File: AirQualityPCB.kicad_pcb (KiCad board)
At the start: 2 copper layers, 100 x 75 mm, 57 parts, among them J1 USB_C_Receptacle_USB2.0_16P, J10 SMA-J-P-H-ST-EM1, J2 TestPoint 5V, J3 TestPoint GND, J4 TestPoint 3.3V, U1 Regulator, U10 INIR2-ME5, U11 110-507, U12 110-303, U13 ESP32-C3-WROOM-02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

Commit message: Updated silkscreen
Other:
- board text added: "LoRa Antenna"
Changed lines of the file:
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@@
+		)
+	)
+	(gr_text "LoRa Antenna"
+		(at 150 65 0)
+		(layer "B.SilkS")
+		(effects
+			(font
+				(size 1.5 1.5)
+				(thickness 0.3)
+				(bold yes)
+			)
+			(justify left bottom mirror)
 		)
 	)

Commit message: Before routing
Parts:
- moved J2 89.5 mm to (296.4, 74.5)
- moved J3 89.5 mm to (292.4, 74.5)
- moved J4 89.5 mm to (288.4, 74.5)
- moved R7 89.5 mm to (284.4, 105.9)
- moved U10 89.5 mm to (255.8, 84.2)
- moved U3 89.5 mm to (276.4, 105.5)
- moved C1 89.5 mm to (243.0, 112.5)
- moved C10 89.5 mm to (279.0, 82.8)
- moved C11 89.5 mm to (220.0, 93.5)
- moved C12 89.5 mm to (244.5, 57.0)
- moved C2 89.5 mm to (230.5, 112.5)
- moved C3 89.5 mm to (262.5, 49.5)
- moved C4 89.5 mm to (267.5, 77.5)
- moved C5 89.5 mm to (255.5, 65.0)
- moved C6 89.5 mm to (252.0, 65.0)
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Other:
- board text added: "Air Quality Monitoring PCB MAE 5220 Designed by Robbie Leslie Cornell University School of Electrical and Computer Engineering School of Mechanical and Aerospace Engineering"
- board text removed: "Air Quality Monitoring PCB Designed by Robbie Leslie Cornell University School of Electrical and Computer Engineering School of Mechanical and Aerospace Engineering"

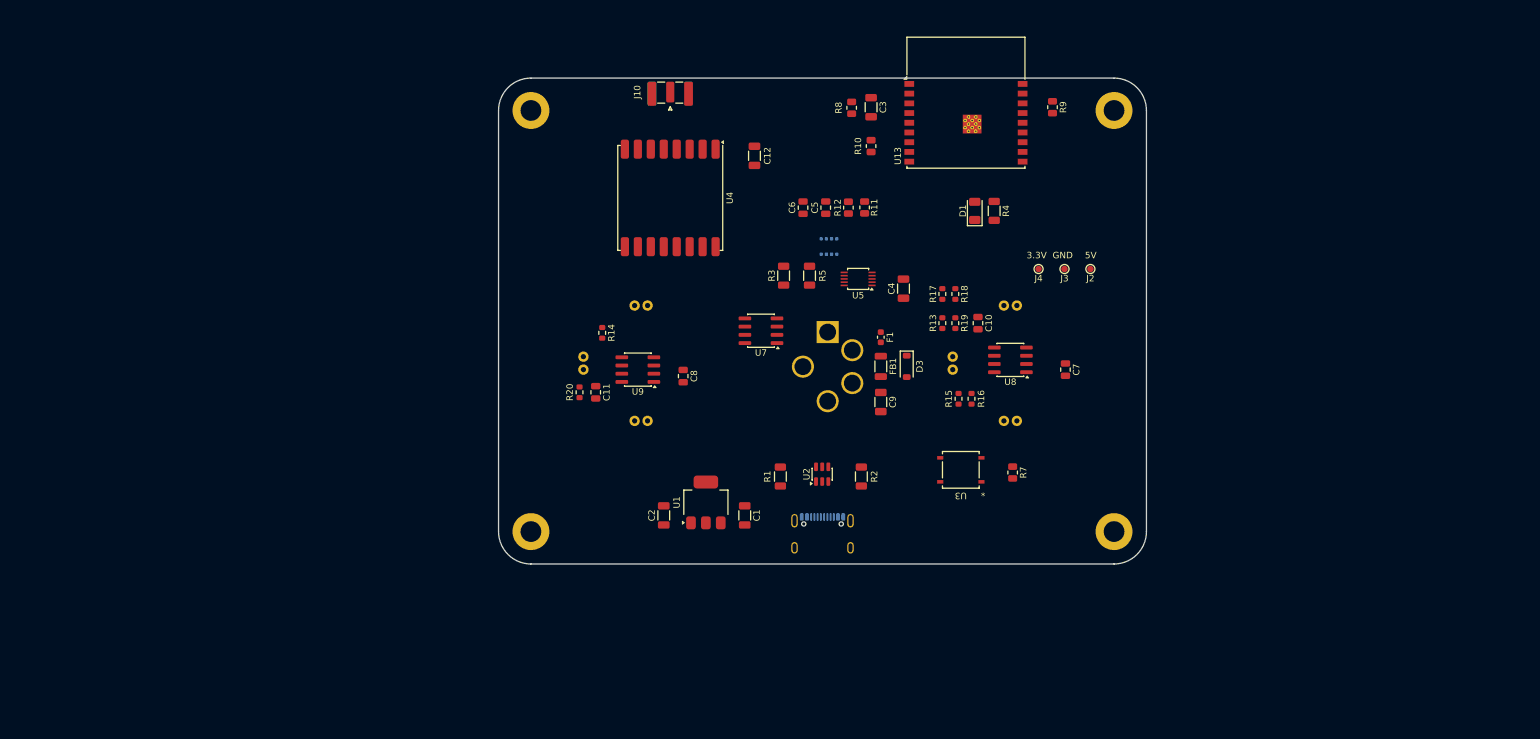
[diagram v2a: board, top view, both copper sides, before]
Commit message: Removed components pre quilter routing
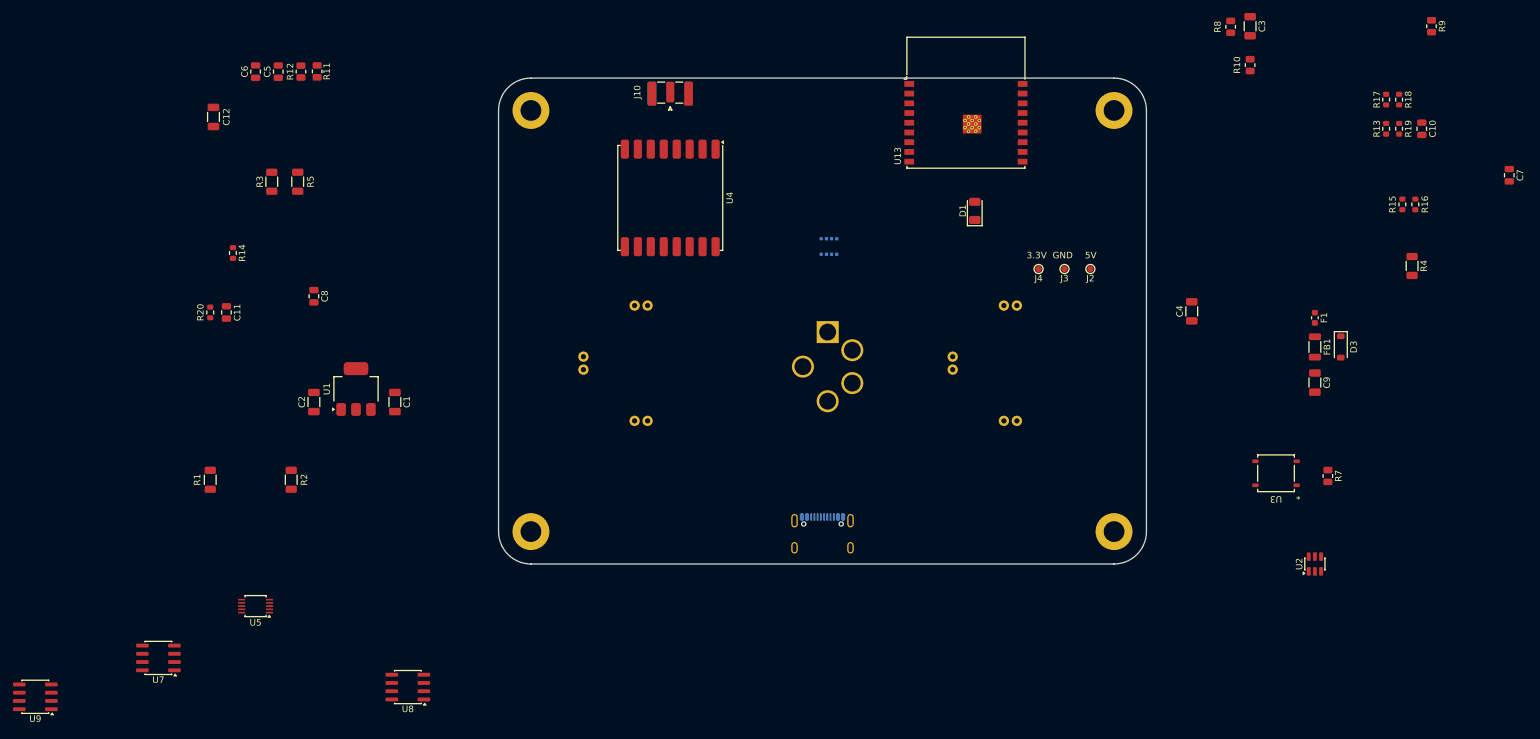
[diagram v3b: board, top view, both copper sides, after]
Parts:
- moved U5 105.8 mm to (167.5, 126.5)
- moved U7 105.8 mm to (152.5, 134.5)
- moved U8 105.8 mm to (191.0, 139.0)
- moved U9 105.8 mm to (133.5, 140.5)
- moved R1 88.0 mm to (160.5, 107.0)
- moved R2 88.0 mm to (173.0, 107.0)
- moved C5 87.1 mm to (171.0, 44.0)
- moved C6 87.1 mm to (167.5, 44.0)
- moved R11 87.1 mm to (177.0, 44.0)
- moved R12 87.1 mm to (174.5, 44.0)
- moved C12 83.7 mm to (161.0, 51.0)
- moved R3 80.3 mm to (170.0, 61.0)
- moved R5 80.3 mm to (174.0, 61.0)
- moved U2 77.3 mm to (331.0, 120.0)
- moved C10 74.8 mm to (347.5, 52.8)
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
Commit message: v1.0 done
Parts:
- moved U2 198.1 mm to (133.0, 112.0)
- moved C10 193.8 mm to (157.1, 88.7)
- moved C7 193.8 mm to (170.6, 95.9)
- moved R13 193.8 mm to (151.6, 88.7)
- moved R15 193.8 mm to (154.1, 100.4)
- moved R16 193.8 mm to (156.1, 100.4)
- moved R17 193.8 mm to (151.6, 84.2)
- moved R18 193.8 mm to (153.6, 84.2)
- moved R19 193.8 mm to (153.6, 88.7)
- moved C9 189.1 mm to (142.1, 100.9)
- moved D3 189.1 mm to (146.1, 95.4)
- moved F1 189.1 mm to (142.1, 90.9)
- moved FB1 189.1 mm to (142.1, 95.4)
- moved R4 186.4 mm to (159.6, 71.4)
- moved C3 181.4 mm to (140.6, 55.4)
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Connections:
- J1 pad S1: unconnected-(J1-SHIELD-PadS1) -> GND
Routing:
- net +3.3V: track 0.00 -> 290.4 mm, vias 0 -> 5
- net VBUS: track 0.00 -> 89.8 mm, vias 0 -> 3
- net /Sensors/Vref: track 0.00 -> 74.3 mm, vias 0 -> 4
- net /D-: track 0.00 -> 68.6 mm
- net /Sensor_RX: track 0.00 -> 67.3 mm, vias 0 -> 1
- net /D+: track 0.00 -> 66.1 mm
- net /DIO1: track 0.00 -> 66.0 mm, vias 0 -> 2
- net /SCK: track 0.00 -> 65.4 mm, vias 0 -> 2
- net /DIO0: track 0.00 -> 65.4 mm, vias 0 -> 2
- net Net-(U13-IO9): track 0.00 -> 63.1 mm, vias 0 -> 4
- net /Sensors/VH2S: track 0.00 -> 61.6 mm, vias 0 -> 2
- net /CS: track 0.00 -> 59.6 mm, vias 0 -> 4
- net /SCL: track 0.00 -> 54.4 mm, vias 0 -> 2
- net /MISO: track 0.00 -> 51.9 mm, vias 0 -> 2
- net /Sensor_TX: track 0.00 -> 50.2 mm, vias 0 -> 2
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- added copper zone on B.Cu, net GND
- added copper zone on F.Cu, net GND
